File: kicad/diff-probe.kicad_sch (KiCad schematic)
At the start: 29 parts, among them IC3 LMH6702, IC4 LMH6702, IC5 LMH6702, J3 HEADER-1X2CARD-EDGE, J4 CON-1X3-TAB-AMP-29173-3-NARROW, X2 SMA--BU-SMA-H

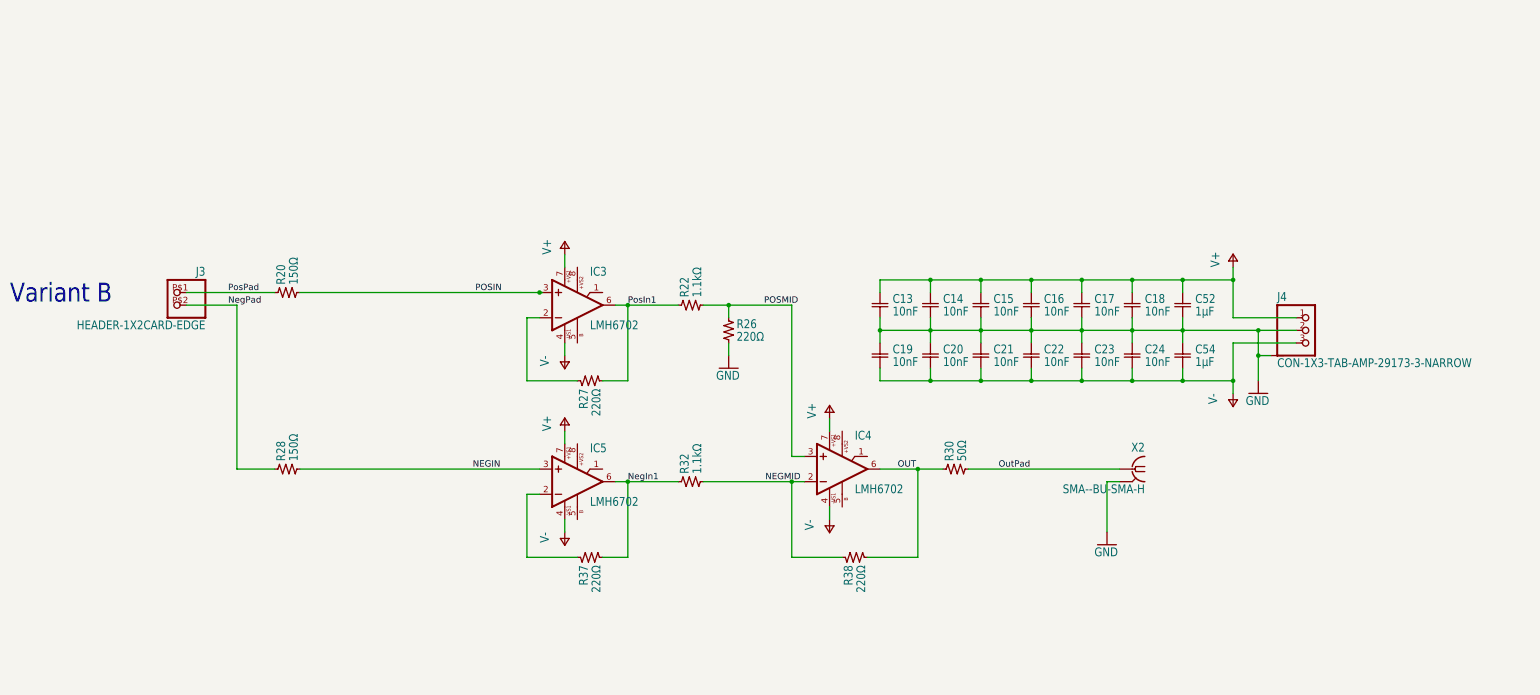
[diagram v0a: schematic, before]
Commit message: Update original project - add the offset generated by the Auto Probe interface. Add the Auto-probe interface PCB.
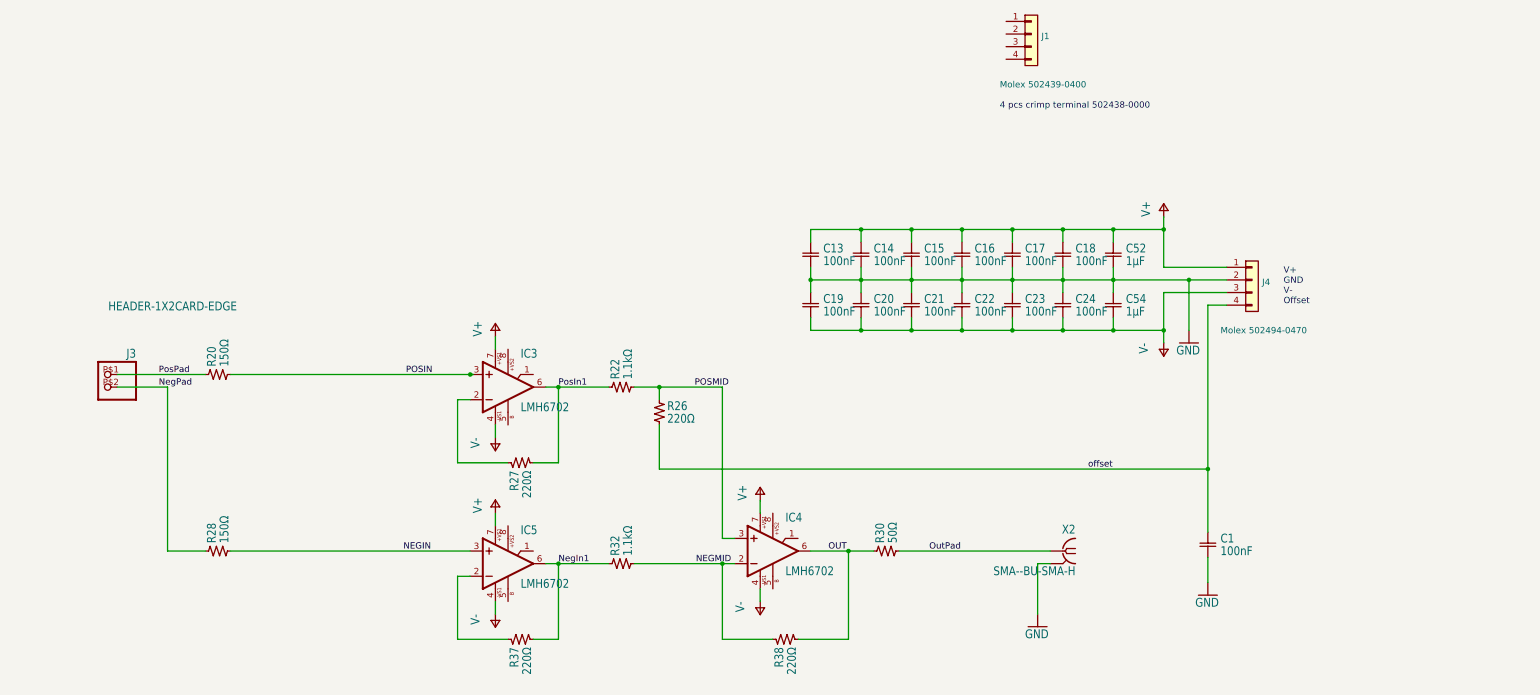
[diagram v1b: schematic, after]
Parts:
- removed J4: CON-1X3-TAB-AMP-29173-3-NARROW, AMP-29173-3-NARROW, symbol diff-probe-eagle-import:CON-1X3-TAB-AMP-29173-3-NARROW
- added C1: 100nF, 0402-SQUARE, symbol diff-probe-eagle-import:C-EU-0402-SQUARE
- added J1: Molex 502439-0400, symbol Connector_Generic:Conn_01x04
- added J4: Molex 502494-0470, Connector_Molex:Molex_CLIK-Mate_502494-0470_1x04-1MP_P2.00mm_Horizontal, symbol Connector_Generic:Conn_01x04
- C13, C14, C15, C16, C17, C18, C19, C20, C21, C22, C23, C24: value 10nF -> 100nF
- X2: footprint BU-SMA-H -> Connector_Coaxial:SMA_Molex_73251-1153_EdgeMount_Horizontal
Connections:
- net GND: now also C1.P$2 (2), J4.2 (Pin_2); no longer R26.P$2 (2)
- net V+: now also J4.1 (Pin_1)
- net V-: now also J4.3 (Pin_3)
- new net offset: C1.P$1 (1), J4.4 (Pin_4), R26.P$2 (2)
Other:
- note added: "4 pcs crimp terminal 502438-0000"
- note added: "V+ GND V- Offset"
- note removed: "Variant B"
- moved on the sheet: C13, C14, C15, C16, C17, C18, C19, C20, C21, C22, C23, C24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
